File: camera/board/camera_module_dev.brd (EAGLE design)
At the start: 48.3 x 38.1 mm, 57 parts, among them IC1 74541PW, IC2 74541PW, Q1 MOSFET-NCHANNELBSS123LT1G, Q2 MOSFET-NCHANNELBSS123LT1G

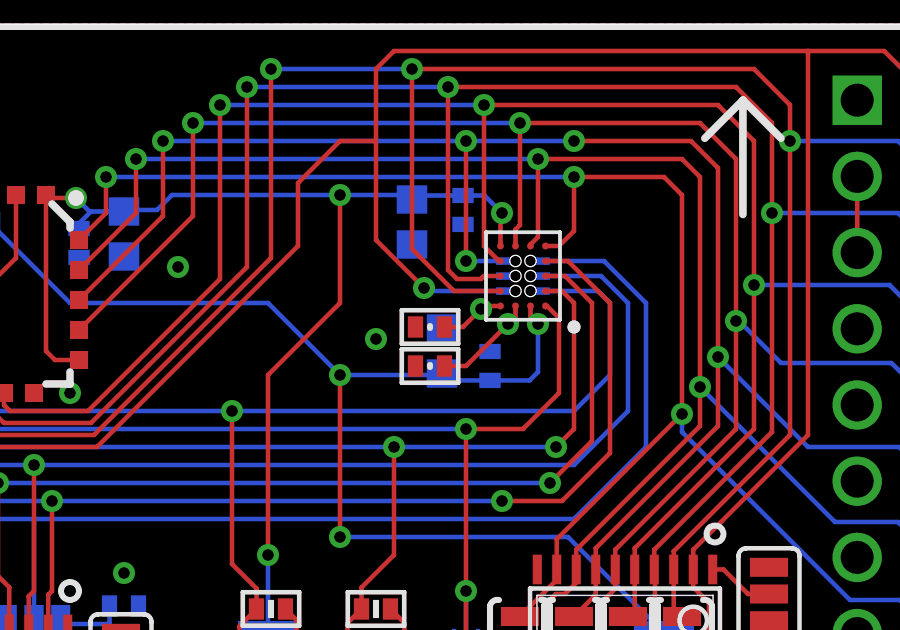
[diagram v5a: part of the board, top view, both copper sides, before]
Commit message: Got rid of holes in 20 csp through package. Preparing for job submission pending spacing check.
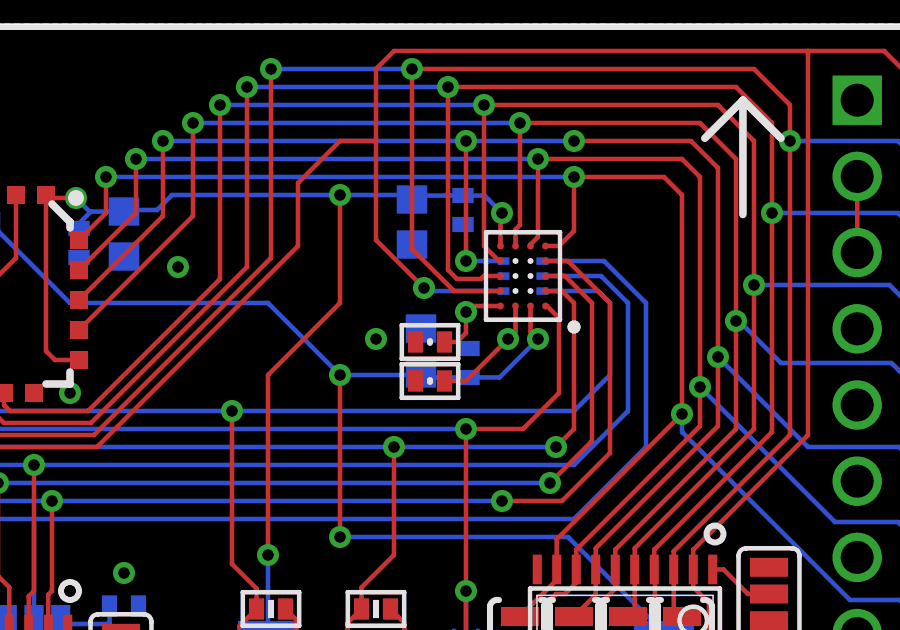
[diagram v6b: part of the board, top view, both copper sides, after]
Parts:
- moved C14 0.71 mm to (27.7, 26.8)
- moved C7 0.70 mm to (26.1, 27.2)
- moved C13 0.50 mm to (26.4, 26.2)
- moved C9 0.50 mm to (26.4, 27.5)
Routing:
- net N$6: track 45.9 -> 45.2 mm
- net N$5: track 2.16 -> 2.77 mm
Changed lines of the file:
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@@
 <layer number="23" name="tOrigins" color="15" fill="1" visible="yes" active="yes"/>
 <layer number="24" name="bOrigins" color="15" fill="1" visible="no" active="yes"/>
-<layer number="25" name="tNames" color="7" fill="1" visible="yes" active="yes"/>
+<layer number="25" name="tNames" color="7" fill="1" visible="no" active="yes"/>
 <layer number="26" name="bNames" color="7" fill="1" visible="no" active="yes"/>
-<layer number="27" name="tValues" color="7" fill="1" visible="yes" active="yes"/>
+<layer number="27" name="tValues" color="7" fill="1" visible="no" active="yes"/>
 <layer number="28" name="bValues" color="7" fill="1" visible="no" active="yes"/>
 <layer number="29" name="tStop" color="7" fill="3" visible="yes" active="yes"/>
@@
 <layer number="49" name="Reference" color="7" fill="1" visible="no" active="yes"/>
 <layer number="50" name="dxf" color="7" fill="1" visible="no" active="no"/>
-<layer number="51" name="tDocu" color="7" fill="1" visible="no" active="yes"/>
+<layer number="51" name="tDocu" color="7" fill="1" visible="yes" active="yes"/>
 <layer number="52" name="bDocu" color="7" fill="1" visible="no" active="yes"/>
 <layer number="53" name="tGND_GNDA" color="7" fill="9" visible="no" active="no"/>
@@
 </element>
 <element name="R11" library="biomimetic" package="0402-RES" value="4k7" x="24.1" y="12.6" smashed="yes"/>
-<element name="C7" library="biomimetic" package="0603-CAP" value="4.7uF" x="26.8" y="27.2" smashed="yes" rot="MR270">
-<attribute name="VOLTAGE" value="6.3V" x="26.8" y="27.2" size="1.778" layer="28" rot="MR270" display="off"/>
-<attribute name="VALUE" x="25.8986" y="28.0494" size="0.8128" layer="28" font="vector" ratio="20" rot="MR270"/>
+<element name="C7" library="biomimetic" package="0603-CAP" value="4.7uF" x="26.1" y="27.2" smashed="yes" rot="MR270">
+<attribute name="VOLTAGE" value="6.3V" x="26.1" y="27.2" size="1.778" layer="28" rot="MR270" display="off"/>
+<attribute name="VALUE" x="25.1986" y="28.0494" size="0.8128" layer="28" font="vector" ratio="20" rot="MR270"/>
 </element>
 <element name="C8" library="biomimetic" package="0402-CAP" value="100nF" x="27.5" y="31.9" smashed="yes" rot="MR270">
@@
 <attribute name="VALUE" x="25.7967" y="33.6954" size="0.8128" layer="28" font="vector" ratio="20" rot="MR180"/>
 </element>
-<element name="C9" library="biomimetic" package="0402-CAP" value="100nF" x="26.4" y="28" smashed="yes" rot="R180">
-<attribute name="VOLTAGE" value="6.3V" x="26.4" y="28" size="1.778" layer="27" rot="R180" display="off"/>
-<attribute name="VALUE" x="25.5046" y="25.7033" size="0.8128" layer="27" font="vector" ratio="20" rot="R270"/>
+<element name="C9" library="biomimetic" package="0402-CAP" value="100nF" x="26.4" y="27.5" smashed="yes" rot="R180">
+<attribute name="VOLTAGE" value="6.3V" x="26.4" y="27.5" size="1.778" layer="27" rot="R180" display="off"/>
+<attribute name="VALUE" x="25.5046" y="25.2033" size="0.8128" layer="27" font="vector" ratio="20" rot="R270"/>
 </element>
 <element name="C10" library="biomimetic" package="0603-CAP" value="4.7uF" x="25.8" y="31.5" smashed="yes" rot="MR270">
@@
 <attribute name="VALUE" x="11.3986" y="36.5494" size="0.8128" layer="28" font="vector" ratio="20" rot="MR270"/>
 </element>
-<element name="C13" library="biomimetic" package="0402-CAP" value="100nF" x="26.4" y="26.7" smashed="yes" rot="R180">
-<attribute name="VOLTAGE" value="6.3V" x="26.4" y="26.7" size="1.778" layer="27" rot="R180" display="off"/>
-</element>
-<element name="C14" library="biomimetic" package="0402-CAP" value="100nF" x="28.4" y="26.7" smashed="yes" rot="MR270">
-<attribute name="VOLTAGE" value="6.3V" x="28.4" y="26.7" size="1.778" layer="28" rot="MR270" display="off"/>
-<attribute name="VALUE" x="29.9954" y="27.3033" size="0.8128" layer="28" font="vector" ratio="20" rot="MR270"/>
+<element name="C13" library="biomimetic" package="0402-CAP" value="100nF" x="26.4" y="26.2" smashed="yes" rot="R180">
+<attribute name="VOLTAGE" value="6.3V" x="26.4" y="26.2" size="1.778" layer="27" rot="R180" display="off"/>
+</element>
+<element name="C14" library="biomimetic" package="0402-CAP" value="100nF" x="27.7" y="26.8" smashed="yes" rot="MR270">
+<attribute name="VOLTAGE" value="6.3V" x="27.7" y="26.8" size="1.778" layer="28" rot="MR270" display="off"/>
+<attribute name="VALUE" x="29.2954" y="27.4033" size="0.8128" layer="28" font="vector" ratio="20" rot="MR270"/>
 </element>
 <element name="C15" library="biomimetic" package="0402-CAP" value="100nF" x="14.7" y="30.8" smashed="yes" rot="MR90">
@@
 <contactref element="C13" pad="1"/>
 <contactref element="U$1" pad="A3"/>
-<via x="29" y="28.1" extent="1-16" drill="0.381"/>
-<wire x1="29.25" y1="28.7" x2="29.25" y2="28.35" width="0.1524" layer="1"/>
-<wire x1="29.25" y1="28.35" x2="29" y2="28.1" width="0.1524" layer="1"/>
-<wire x1="29" y1="28.1" x2="28.9826" y2="28.0826" width="0.1524" layer="1"/>
-<wire x1="26.8826" y1="26.7" x2="27.6" y2="26.7" width="0.1524" layer="1"/>
-<wire x1="27.6" y1="26.7" x2="29" y2="28.1" width="0.1524" layer="1"/>
+<via x="29" y="27.6" extent="1-16" drill="0.381"/>
+<wire x1="29.25" y1="28.7" x2="29.25" y2="27.85" width="0.1524" layer="1"/>
+<wire x1="29.25" y1="27.85" x2="29" y2="27.6" width="0.1524" layer="1"/>
+<wire x1="26.8826" y1="26.2" x2="27.6" y2="26.2" width="0.1524" layer="1"/>
+<wire x1="27.6" y1="26.2" x2="29" y2="27.6" width="0.1524" layer="1"/>
 </signal>
 <signal name="N$5">
 <contactref element="U$1" pad="A4"/>
 <contactref element="C9" pad="1"/>
-<via x="28.1" y="28.6" extent="1-16" drill="0.381"/>
-<wire x1="28.75" y1="28.7" x2="28.2" y2="28.7" width="0.1524" layer="1"/>
-<wire x1="28.2" y1="28.7" x2="28.1" y2="28.6" width="0.1524" layer="1"/>
-<wire x1="26.8826" y1="28" x2="27.5" y2="28" width="0.1524" layer="1"/>
-<wire x1="27.5" y1="28" x2="28.1" y2="28.6" width="0.1524" layer="1"/>
+<via x="27.6" y="28.5" extent="1-16" drill="0.381"/>
+<wire x1="28.75" y1="28.7" x2="27.8" y2="28.7" width="0.1524" layer="1"/>
+<wire x1="27.8" y1="28.7" x2="27.6" y2="28.5" width="0.1524" layer="1"/>
+<wire x1="27.6" y1="28.5" x2="27.6" y2="27.8" width="0.1524" layer="1"/>
+<wire x1="27.6" y1="27.8" x2="27.3" y2="27.5" width="0.1524" layer="1"/>
+<wire x1="27.3" y1="27.5" x2="26.8826" y2="27.5" width="0.1524" layer="1"/>
 </signal>
 <signal name="N$6">
@@
 <contactref element="C12" pad="1"/>
 <contactref element="C16" pad="1"/>
-<via x="30" y="28.1" extent="1-16" drill="0.381"/>
-<wire x1="29.75" y1="28.7" x2="29.75" y2="28.35" width="0.1524" layer="1"/>
-<wire x1="29.75" y1="28.35" x2="30" y2="28.1" width="0.1524" layer="1"/>
+<via x="30" y="27.6" extent="1-16" drill="0.381"/>
 <wire x1="34.2" y1="17.8" x2="31" y2="21" width="0.1524" layer="16"/>
 <wire x1="31" y1="21" x2="23.4" y2="21" width="0.1524" layer="16"/>
@@
 <wire x1="23.4" y1="21" x2="23.4" y2="26.4" width="0.1524" layer="1"/>
 <via x="23.4" y="26.4" extent="1-16" drill="0.381"/>
-<wire x1="23.4" y1="26.4" x2="26.7493" y2="26.4" width="0.1524" layer="16"/>
-<wire x1="26.7493" y1="26.4" x2="26.8" y2="26.4507" width="0.1524" layer="16"/>
-<wire x1="28.4" y1="26.2174" x2="27.0333" y2="26.2174" width="0.1524" layer="16"/>
-<wire x1="27.0333" y1="26.2174" x2="26.8" y2="26.4507" width="0.1524" layer="16"/>
-<wire x1="28.4" y1="26.2174" x2="29.7174" y2="26.2174" width="0.1524" layer="16"/>
-<wire x1="29.7174" y1="26.2174" x2="30" y2="26.5" width="0.1524" layer="16"/>
-<wire x1="30" y1="26.5" x2="30" y2="28.1" width="0.1524" layer="16"/>
 <via x="8.1" y="32.4" extent="1-16" drill="0.381"/>
 <wire x1="8.1" y1="32.4" x2="8.1" y2="31.3" width="0.1524" layer="1"/>
@@
 <wire x1="9.3" y1="32.3826" x2="10.5667" y2="32.3826" width="0.1524" layer="16"/>
 <wire x1="10.5667" y1="32.3826" x2="10.8" y2="32.1493" width="0.1524" layer="16"/>
+<wire x1="29.75" y1="28.7" x2="29.75" y2="27.85" width="0.1524" layer="1"/>
+<wire x1="29.75" y1="27.85" x2="30" y2="27.6" width="0.1524" layer="1"/>
+<wire x1="23.4" y1="26.4" x2="26.0493" y2="26.4" width="0.1524" layer="16"/>
+<wire x1="26.0493" y1="26.4" x2="26.1" y2="26.4507" width="0.1524" layer="16"/>
+<wire x1="27.7" y1="26.3174" x2="26.2333" y2="26.3174" width="0.1524" layer="16"/>
+<wire x1="26.2333" y1="26.3174" x2="26.1" y2="26.4507" width="0.1524" layer="16"/>
+<wire x1="27.7" y1="26.3174" x2="28.7174" y2="26.3174" width="0.1524" layer="16"/>
+<wire x1="28.7174" y1="26.3174" x2="30" y2="27.6" width="0.1524" layer="16"/>
 </signal>
 <signal name="N$8">

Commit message: Board and component orders placed
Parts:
- C10, C11, C12, C7: value 4.7uF -> 10uF
- R2: value 18k/5k -> 18k/5k1
- R5: value (none) -> 10k
- R6: value 1k8 -> 2k
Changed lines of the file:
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@@
 <attribute name="VALUE" x="25.3046" y="18.1967" size="0.8128" layer="28" font="vector" ratio="20" rot="MR90"/>
 </element>
-<element name="R2" library="biomimetic" package="0402-RES" value="18k/5k" x="32.1" y="16.8" smashed="yes" rot="MR90">
+<element name="R2" library="biomimetic" package="0402-RES" value="18k/5k1" x="32.1" y="16.8" smashed="yes" rot="MR90">
 <attribute name="VALUE" x="31.857" y="18.1205" size="0.8128" layer="28" font="vector" ratio="20" rot="MR90"/>
 </element>
@@
 <element name="C3" library="biomimetic" package="0402-CAP" value="1uF" x="29.5" y="16.8" smashed="yes" rot="MR90">
 <attribute name="VALUE" x="29.3046" y="18.0967" size="0.8128" layer="28" font="vector" ratio="20" rot="MR90"/>
+<attribute name="VOLTAGE" value="6.3V" x="29.5" y="16.8" size="1.778" layer="28" rot="MR90" display="off"/>
 </element>
 <element name="R1" library="biomimetic" package="0402-RES" value="18k" x="23.1" y="16.8" smashed="yes" rot="MR90">
@@
 <attribute name="VALUE" x="24.157" y="18.0205" size="0.8128" layer="28" font="vector" ratio="20" rot="MR90"/>
 </element>
-<element name="R5" library="biomimetic" package="0402-RES" value="" x="28.8" y="14.4" smashed="yes" rot="MR180">
+<element name="R5" library="biomimetic" package="0402-RES" value="10k" x="28.8" y="14.4" smashed="yes" rot="MR180">
 <attribute name="VALUE" x="27.8205" y="15.743" size="0.6096" layer="28" font="vector" ratio="25" rot="MR180"/>
 </element>
@@
 <attribute name="VALUE" x="41.8033" y="13.2954" size="0.8128" layer="27" font="vector" ratio="20" rot="R180"/>
 </element>
-<element name="R6" library="biomimetic" package="0402-RES" value="1k8" x="16.2" y="17.4" smashed="yes" rot="MR180">
+<element name="R6" library="biomimetic" package="0402-RES" value="2k" x="16.2" y="17.4" smashed="yes" rot="MR180">
 <attribute name="VALUE" x="17.3205" y="18.143" size="0.8128" layer="28" font="vector" ratio="20" rot="MR180"/>
 </element>
@@
 </element>
 <element name="R11" library="biomimetic" package="0402-RES" value="4k7" x="24.1" y="12.6" smashed="yes"/>
-<element name="C7" library="biomimetic" package="0603-CAP" value="4.7uF" x="26.1" y="27.2" smashed="yes" rot="MR270">
+<element name="C7" library="biomimetic" package="0603-CAP" value="10uF" x="26.1" y="27.2" smashed="yes" rot="MR270">
 <attribute name="VOLTAGE" value="6.3V" x="26.1" y="27.2" size="1.778" layer="28" rot="MR270" display="off"/>
 <attribute name="VALUE" x="25.1986" y="28.0494" size="0.8128" layer="28" font="vector" ratio="20" rot="MR270"/>
@@
 <attribute name="VALUE" x="25.5046" y="25.2033" size="0.8128" layer="27" font="vector" ratio="20" rot="R270"/>
 </element>
-<element name="C10" library="biomimetic" package="0603-CAP" value="4.7uF" x="25.8" y="31.5" smashed="yes" rot="MR270">
+<element name="C10" library="biomimetic" package="0603-CAP" value="10uF" x="25.8" y="31.5" smashed="yes" rot="MR270">
 <attribute name="VOLTAGE" value="6.3V" x="25.8" y="31.5" size="1.778" layer="28" rot="MR270" display="off"/>
 <attribute name="VALUE" x="24.6986" y="32.9494" size="0.8128" layer="28" font="vector" ratio="20" rot="MR270"/>
 </element>
-<element name="C11" library="biomimetic" package="0603-CAP" value="4.7uF" x="16.2" y="31.1" smashed="yes" rot="MR90">
+<element name="C11" library="biomimetic" package="0603-CAP" value="10uF" x="16.2" y="31.1" smashed="yes" rot="MR90">
 <attribute name="VOLTAGE" value="6.3V" x="16.2" y="31.1" size="1.778" layer="28" rot="MR90" display="off"/>
 <attribute name="VALUE" x="15.8014" y="26.1506" size="0.8128" layer="28" font="vector" ratio="20" rot="MR90"/>
 </element>
-<element name="C12" library="biomimetic" package="0603-CAP" value="4.7uF" x="10.8" y="31.4" smashed="yes" rot="MR270">
+<element name="C12" library="biomimetic" package="0603-CAP" value="10uF" x="10.8" y="31.4" smashed="yes" rot="MR270">
 <attribute name="VOLTAGE" value="6.3V" x="10.8" y="31.4" size="1.778" layer="28" rot="MR270" display="off"/>
 <attribute name="VALUE" x="11.3986" y="36.5494" size="0.8128" layer="28" font="vector" ratio="20" rot="MR270"/>
